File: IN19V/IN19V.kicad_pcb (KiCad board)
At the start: 2 copper layers, 18 x 18 mm, 16 parts

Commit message: Add files via upload
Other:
- board text added: "this side up"
- board text added: "tube side"
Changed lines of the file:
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@@
   (general
     (thickness 1.6)
-    (drawings 3)
+    (drawings 5)
     (tracks 46)
     (zones 0)
@@
     (tags "solder jumper open")
     (attr virtual)
-    (fp_text reference Π (at 1.344197 0.036976 233) (layer F.SilkS)
+    (fp_text reference Π (at 1.344197 0.036976 233 unlocked) (layer F.SilkS)
       (effects (font (size 0.5 0.5) (thickness 0.125)))
     )
@@
     (tags "solder jumper open")
     (attr virtual)
-    (fp_text reference A/B (at 1.389419 0.070487 253) (layer F.SilkS)
+    (fp_text reference A/B (at 1.389419 0.070487 253 unlocked) (layer F.SilkS)
       (effects (font (size 0.5 0.5) (thickness 0.125)))
     )
@@
     (tags "solder jumper open")
     (attr virtual)
-    (fp_text reference < (at 1.306994 0.081471 320) (layer F.SilkS)
+    (fp_text reference < (at 1.306994 0.081471 140 unlocked) (layer F.SilkS)
       (effects (font (size 0.5 0.5) (thickness 0.125)))
     )
@@
     (tags "solder jumper open")
     (attr virtual)
-    (fp_text reference > (at 1.314888 0.227065 61) (layer F.SilkS)
+    (fp_text reference > (at 1.314888 0.227065 241 unlocked) (layer F.SilkS)
       (effects (font (size 0.5 0.5) (thickness 0.125)))
     )
@@
     (tags "solder jumper open")
     (attr virtual)
-    (fp_text reference dB (at 1.280639 0.063146 125) (layer F.SilkS)
+    (fp_text reference dB (at 1.280639 0.063146 125 unlocked) (layer F.SilkS)
       (effects (font (size 0.5 0.5) (thickness 0.125)))
     )
@@
       (net 1 "Net-(J1-Pad1)"))
   )
+  (gr_text "this\nside\nup" (at 70.02526 110.51286) (layer F.SilkS)
+    (effects (font (size 0.6 0.6) (thickness 0.125)))
+  )
+  (gr_text "tube\nside" (at 68.04406 108.25226) (layer B.SilkS)
+    (effects (font (size 0.5 0.5) (thickness 0.125)) (justify mirror))
+  )
   (gr_text "layout by\nAnalogTek" (at 68.00342 110.52302) (layer B.SilkS)

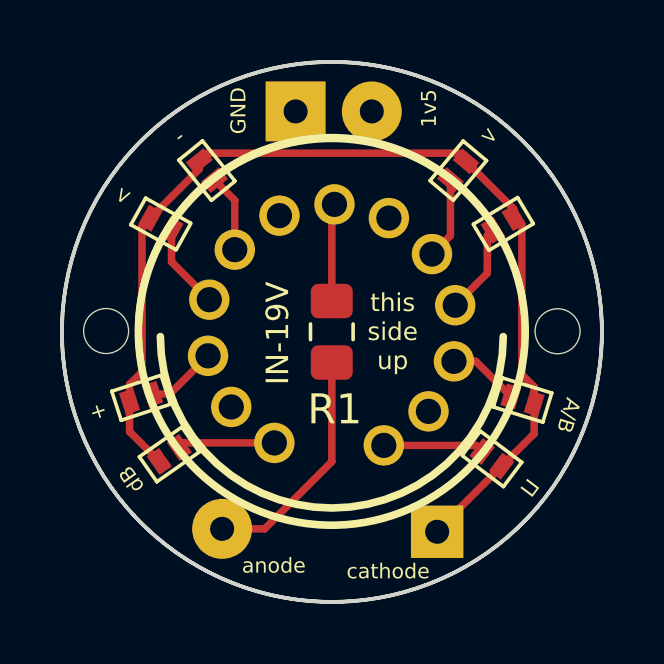
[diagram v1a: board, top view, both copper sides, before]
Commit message: Add files via upload
15 NOV 2020 11:06 PM changed trace width from .25mm to .4 - .75mm.
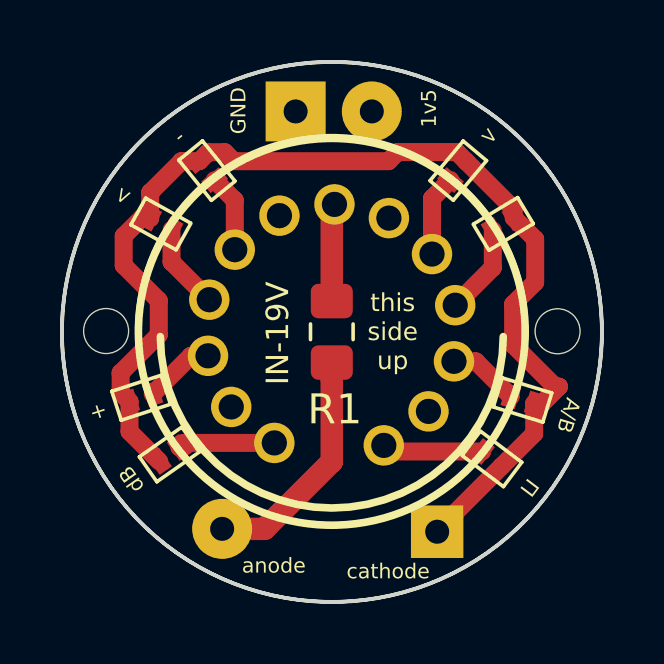
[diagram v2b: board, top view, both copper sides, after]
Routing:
- net Net-(J2-Pad1): track 35.1 -> 38.7 mm
